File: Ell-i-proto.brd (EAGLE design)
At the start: 99 x 53.3 mm, 139 parts, among them J1 FTDI-SER-6, J10 PJ-102AX, J2 PWMH, J3 PWR, J4 PWML, J5 ANAL, J6 SPI, J7 COMM, J8 ANAH, J9 RJ45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

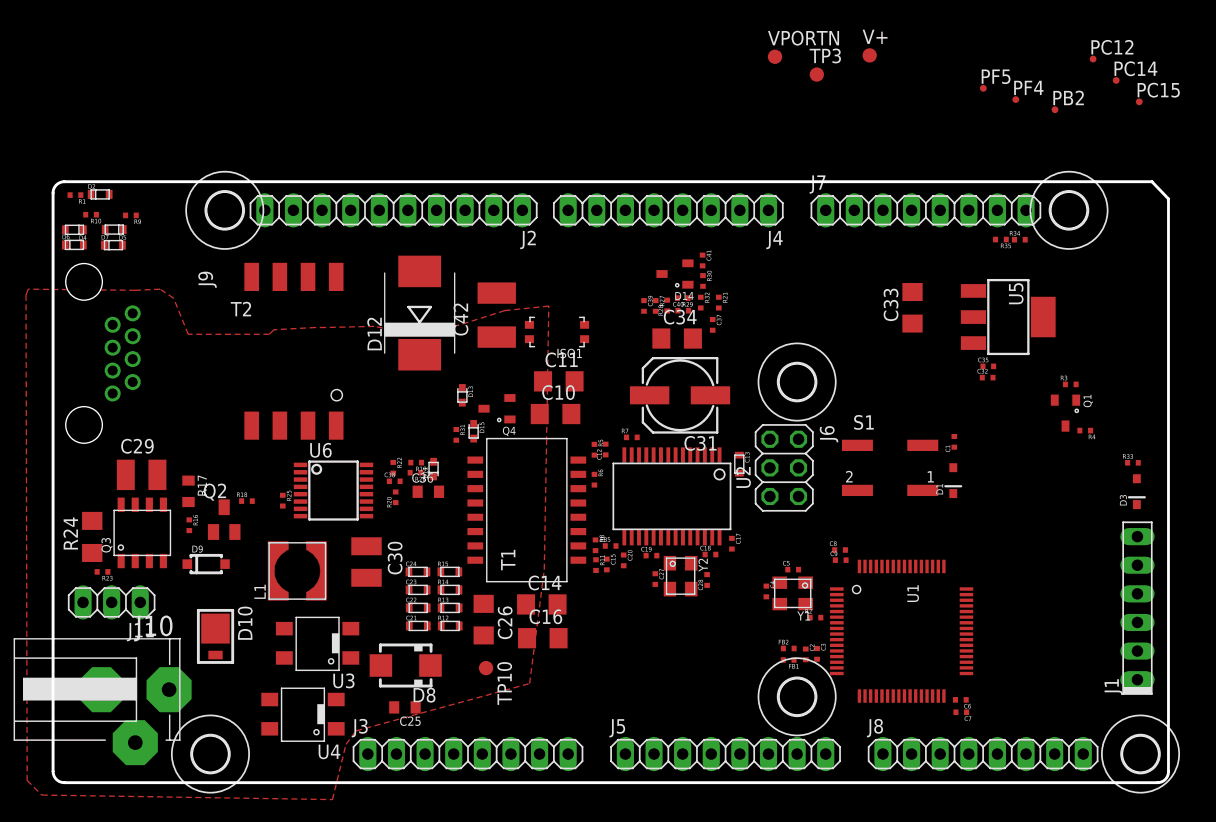
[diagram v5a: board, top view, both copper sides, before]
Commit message: pushbutton and power LED to the right edge, some more drafting
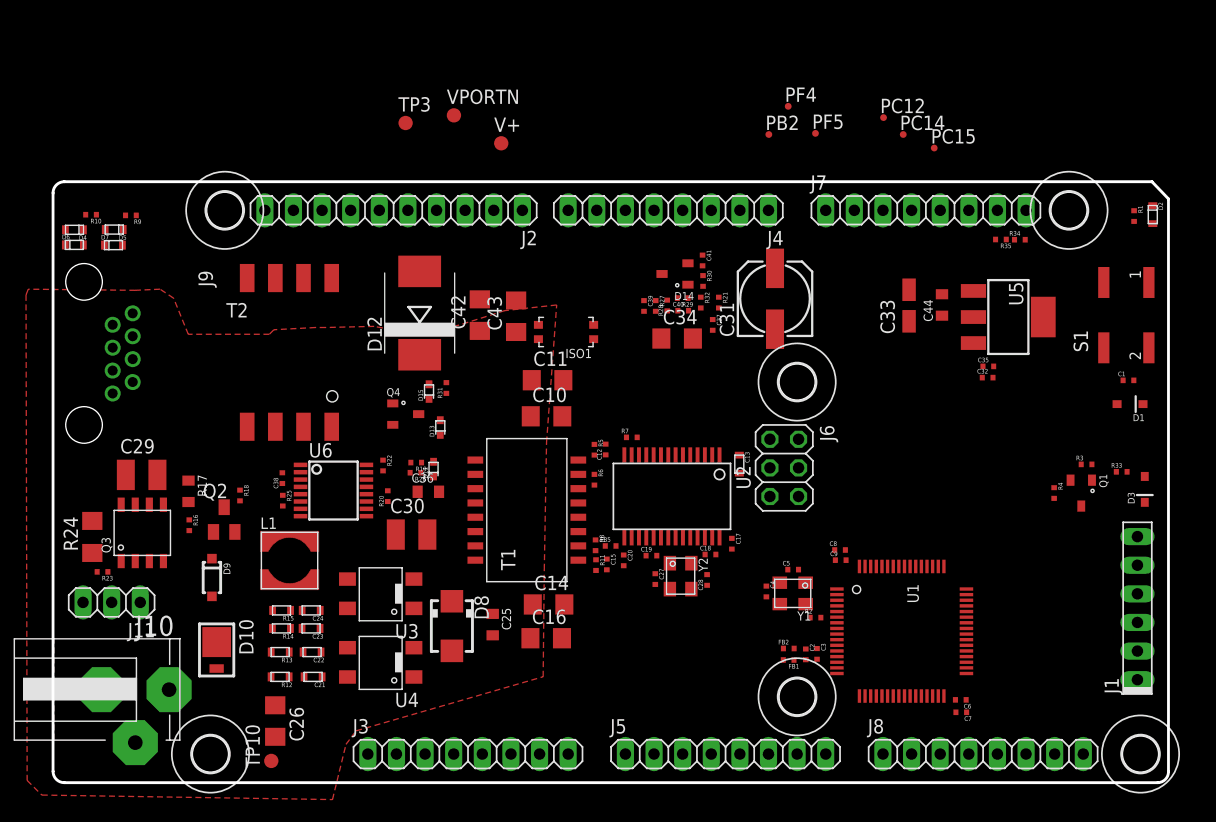
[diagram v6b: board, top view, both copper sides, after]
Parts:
- added C43: 1n 2kV, rcl:C1206
- added C44: 22u, ell-i:0805
- C33: value 47uF -> opt tant; device rcl:C1206 -> rcl:CT3216
- C42: value 2n2 -> 1n 2kV; device rcl:C1812 -> rcl:C1206
- moved R1 94.0 mm to (96.0, 50.3), turned to 270 degrees
- moved D2 93.4 mm to (97.6, 50.4), turned to 270 degrees
- moved TP3 36.8 mm to (31.3, 58.5)
- moved V+ 33.6 mm to (39.8, 56.8)
- moved VPORTN 29.0 mm to (35.6, 59.2)
- moved PB2 25.5 mm to (63.5, 57.5)
- moved S1 25.0 mm to (95.3, 41.5), turned to 90 degrees
- moved TP10 20.8 mm to (19.4, 1.93), turned to 90 degrees
- moved C26 20.6 mm to (19.7, 5.47)
- moved PF4 20.2 mm to (65.2, 60.0)
- moved PC14 19.5 mm to (75.5, 57.5)
- moved PC12 19.3 mm to (73.7, 59.0)
- moved PC15 18.7 mm to (78.2, 56.3)
- moved D1 17.1 mm to (95.6, 33.6), turned to 180 degrees
- moved C1 16.4 mm to (95.5, 35.7), turned to 0 degrees
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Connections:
- net +3V3: now also C33.+, C44.1; no longer C33.1
- net GND: now also C43.1
- net GNDI: now also C33.-, C43.2, C44.2; no longer C33.2

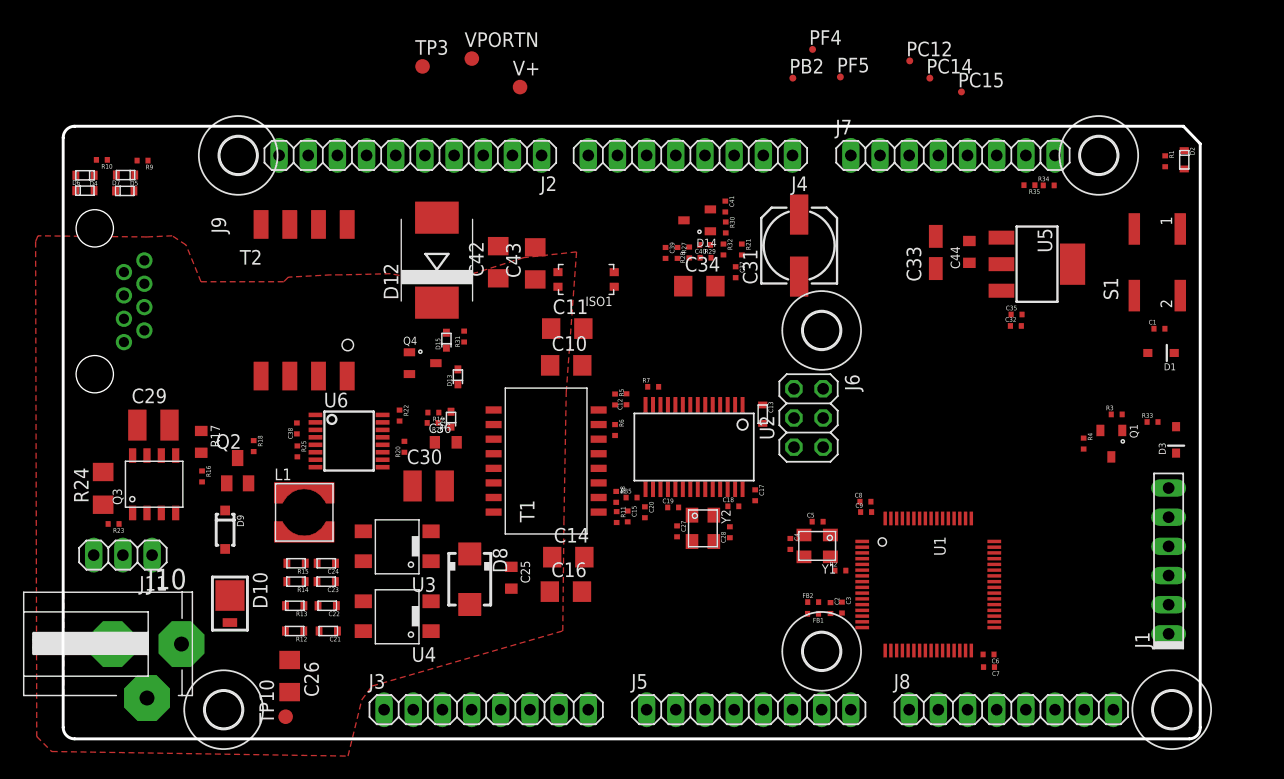
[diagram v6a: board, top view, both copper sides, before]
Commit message: component placement closer to reality..
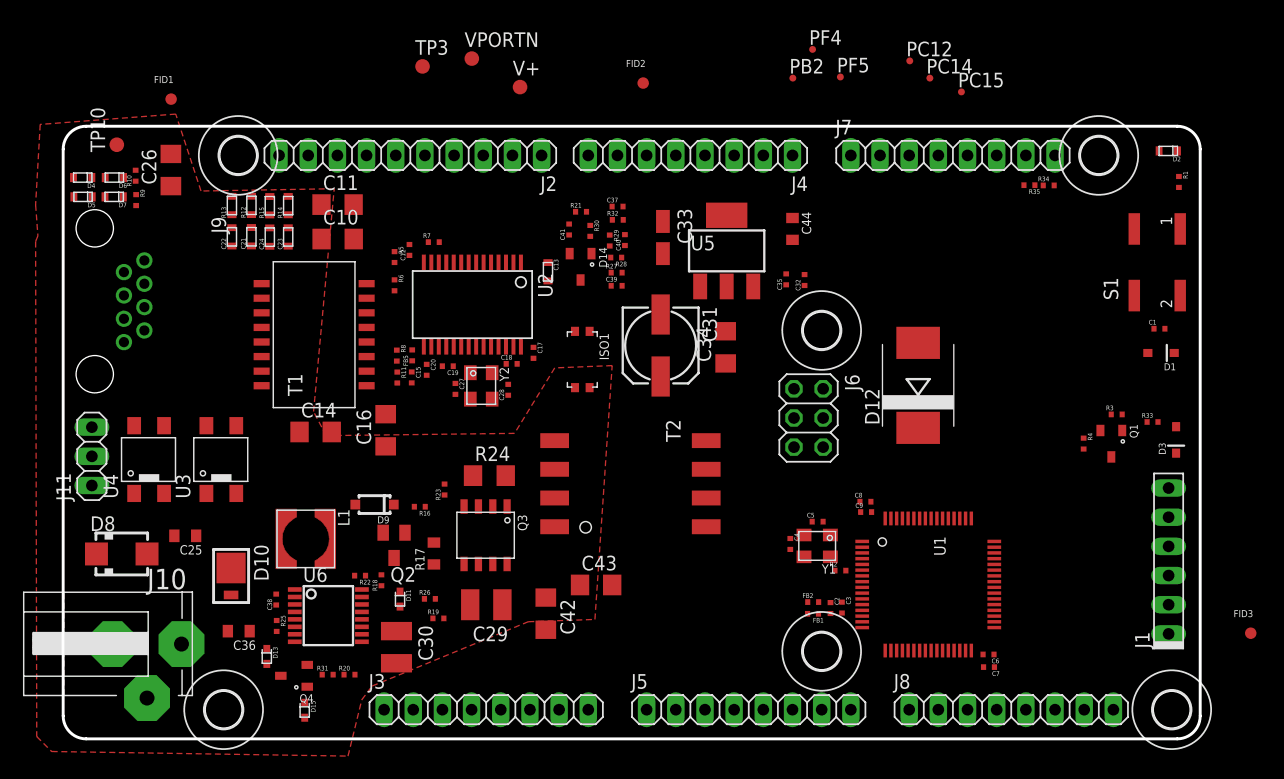
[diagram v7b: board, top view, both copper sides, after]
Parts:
- added FID1, FID2, FID3: MOUNT_FIDUCIAL, ell-i:MOUNT_FIDUCIAL
- moved TP10 51.9 mm to (4.67, 51.7)
- moved C26 45.3 mm to (9.38, 49.5), turned to 90 degrees
- moved D12 43.3 mm to (74.4, 30.8)
- moved R12 37.3 mm to (16.4, 46.5), turned to 90 degrees
- moved R13 35.3 mm to (14.7, 46.4), turned to 90 degrees
- moved C21 35.0 mm to (16.4, 43.7), turned to 90 degrees
- moved D15 34.5 mm to (21.0, 2.49), turned to 270 degrees
- moved R24 33.6 mm to (37.1, 22.9), turned to 0 degrees
- moved C22 33.2 mm to (14.7, 43.7), turned to 90 degrees
- moved C29 32.9 mm to (36.8, 11.7), turned to 180 degrees
- moved R14 32.7 mm to (19.6, 46.4), turned to 90 degrees
- moved T2 32.6 mm to (49.4, 22.2), turned to 270 degrees
- moved R31 31.7 mm to (23.0, 5.59), turned to 0 degrees
- moved R15 31.2 mm to (18.0, 46.4), turned to 90 degrees
- moved C42 30.9 mm to (42.0, 10.9), turned to 270 degrees
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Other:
- outline, holes or cut-outs redrawn

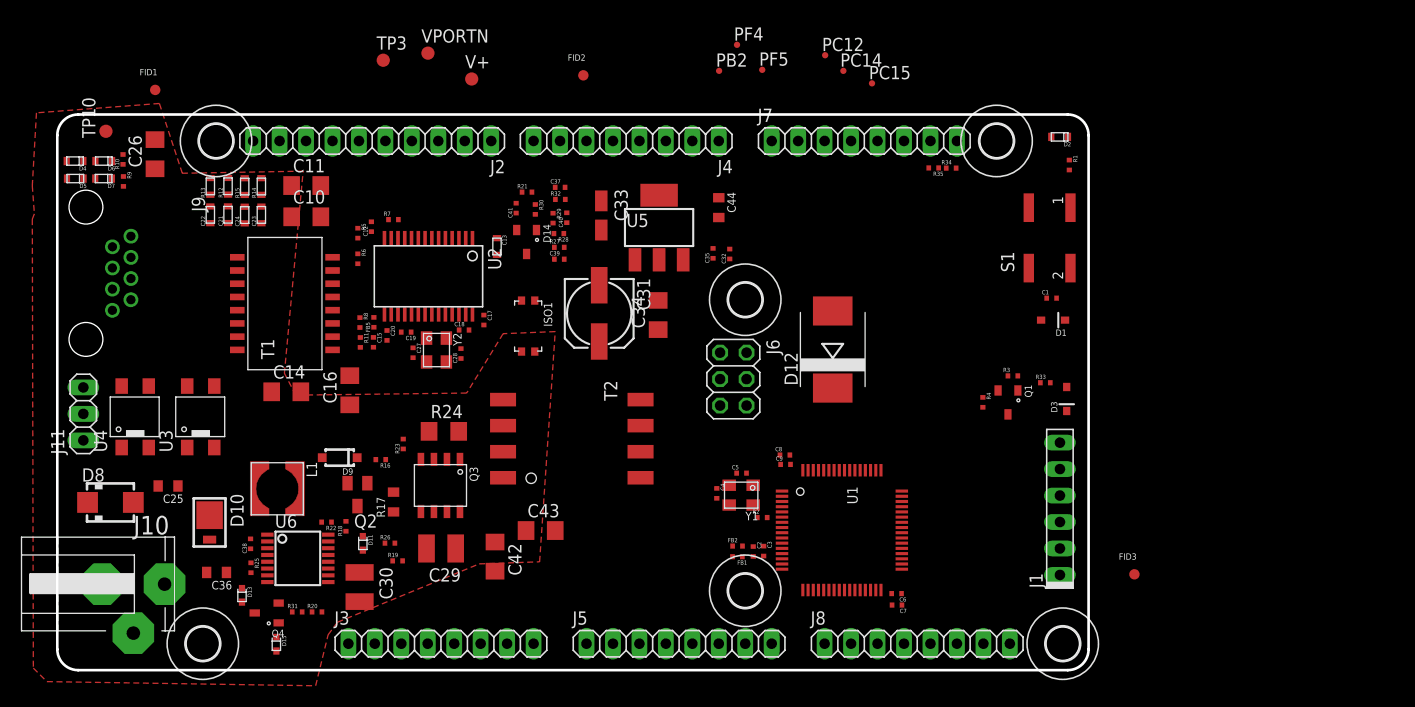
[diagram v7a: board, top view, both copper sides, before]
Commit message: drafting the gnd/power planes in inner layers, some routing, ADCs etc
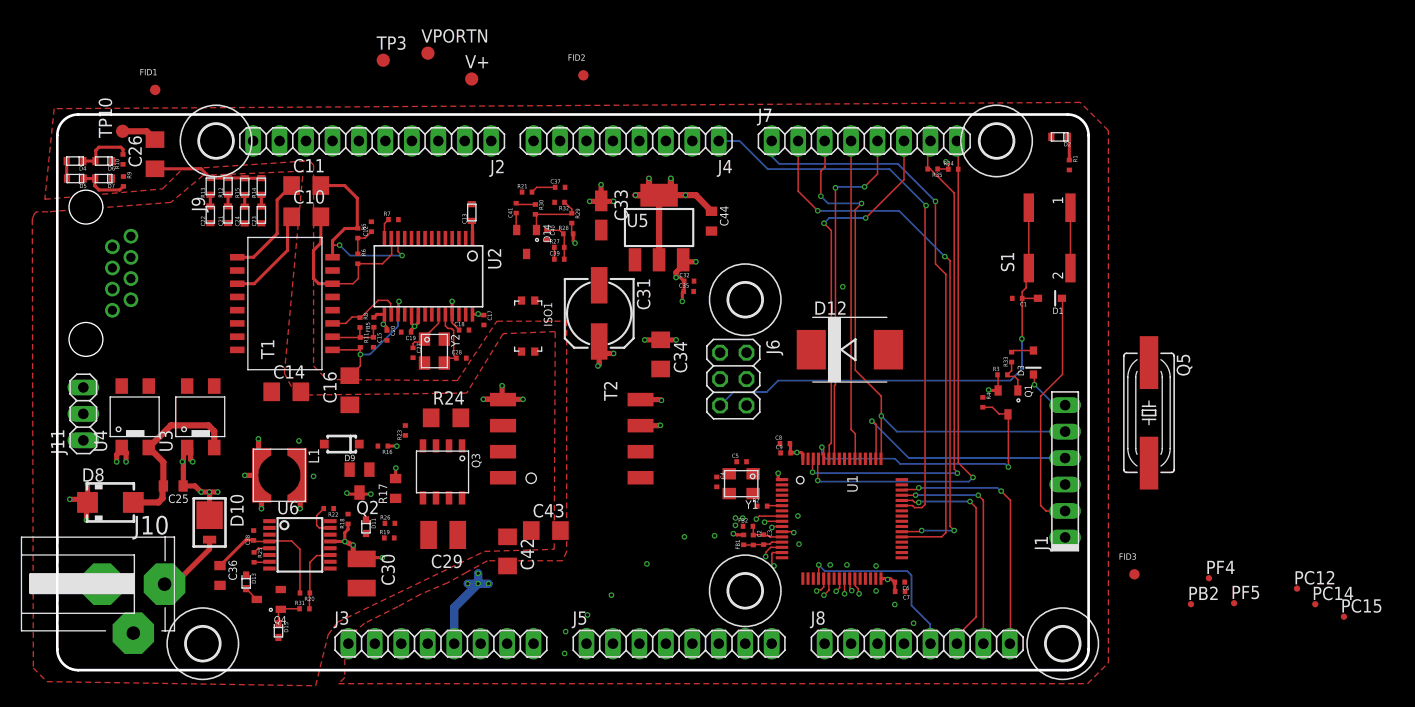
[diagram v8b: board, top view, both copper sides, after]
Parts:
- added Q5: (no value), crystal:SM49
- moved PB2 68.4 mm to (108.8, 6.33)
- moved PC12 68.4 mm to (119.0, 7.83)
- moved PC14 68.4 mm to (120.8, 6.33)
- moved PC15 68.4 mm to (123.5, 5.13)
- moved PF4 68.4 mm to (110.5, 8.83)
- moved PF5 68.4 mm to (113.0, 6.43)
- moved D3 4.74 mm to (93.7, 29.5)
- moved C32 4.69 mm to (60.6, 37.4), turned to 0 degrees
- moved C35 4.34 mm to (60.6, 36.4), turned to 0 degrees
- moved R33 4.07 mm to (91.6, 30.1), turned to 90 degrees
- moved C13 4.06 mm to (39.8, 43.9), turned to 90 degrees
- moved C34 3.79 mm to (57.9, 30.3), turned to 270 degrees
- moved J1 3.63 mm to (96.7, 19.1)
- moved C1 3.30 mm to (92.2, 35.7), turned to 180 degrees
- moved C40 2.54 mm to (47.0, 41.8), turned to 270 degrees
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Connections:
- net AD4: now also U1.14; no longer U1.21
- net AD5: now also U1.15; no longer U1.22
- net AD6: now also U1.21; no longer U1.14
- net AD7: now also U1.22; no longer U1.15
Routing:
- net SPR1: track 0.00 -> 55.6 mm, vias 0 -> 1
- net TX2: track 0.00 -> 53.7 mm, vias 0 -> 3
- net RX1: track 0.00 -> 53.6 mm, vias 0 -> 1
- net SPR2: track 0.00 -> 53.3 mm, vias 0 -> 4
- net SCL1: track 0.00 -> 50.1 mm, vias 0 -> 2
- net +3V3: track 0.00 -> 49.3 mm, vias 0 -> 17
- net SDA1: track 0.00 -> 48.6 mm, vias 0 -> 2
- net NRES: track 0.00 -> 47.7 mm, vias 0 -> 1
- net PB7: track 0.00 -> 36.1 mm, vias 0 -> 2
- net PB6: track 0.00 -> 33.8 mm, vias 0 -> 2
- net V+: track 0.00 -> 32.9 mm, vias 0 -> 13
- net +5V: track 0.00 -> 32.9 mm, vias 0 -> 14
- net PD2: track 0.00 -> 30.7 mm
- net N118561: track 0.00 -> 28.0 mm, vias 0 -> 2
- net SWD: track 0.00 -> 24.8 mm, vias 0 -> 2
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- added copper zone on layer 2, net +3V3
- added copper zone on layer 2, net +5V
- added copper zone on layer 15, net GND
- added copper zone on layer 1, net GNDI
- added copper zone on layer 15, net GNDI
- added copper zone on layer 2, net N62909
- added copper zone on layer 2, net V+
